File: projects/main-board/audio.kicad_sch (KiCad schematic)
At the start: 12 parts

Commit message: Updated schematics with new symbols
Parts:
- removed U10: ~, symbol symbol-library:NAU8325YG
- added U6: NAU8325YG, footprint-library:NAU8325YG, symbol symbol-library:NAU8325YG
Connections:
- net 1V8: now also U6.5 (A_VDD)
- net 3V3: now also U6.14 (SPK_VDD), U6.18 (SPK_VDD), U6.2 (SPK_VDD), U6.9 (IO_VDD)
- net GND: now also U6.13 (IO_GND), U6.16 (SPK_GND), U6.20 (SPK_GND), U6.21 (PAD), U6.3 (A_GND)
- net I2C.SCL: now also U6.11 (SCL)
- net I2C.SDA: now also U6.12 (SDA)
- net I2S.BCK: now also U6.8 (BCK)
- net I2S.DACDAT: now also U6.7 (DACDAT)
- net I2S.LRCK: now also U6.6 (LRCK)
- net I2S.MCLK: now also U6.10 (MCLK)
- net at C98.1: now also U6.4 (VREF)
- net at LS1.1: now also U6.15 (SPK_LP)
- net at LS1.2: now also U6.17 (SPK_LN)
- net at LS2.2: now also U6.1 (SPK_RP)
- net at LS2.1: now also U6.19 (SPK_RN)
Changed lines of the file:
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@@
+	)
+	(symbol
+		(lib_name "NAU8325YG_1")
+		(lib_id "symbol-library:NAU8325YG")
+		(at 152.4 63.5 0)
+		(unit 1)
+		(exclude_from_sim no)
+		(in_bom yes)
+		(on_board yes)
+		(dnp no)
+		(property "Reference" "U6"
+			(at 153.67 62.23 0)
+			(effects
+				(font
+					(size 1.27 1.27)
+				)
+			)
+		)
+		(property "Value" "NAU8325YG"
+			(at 157.48 129.54 0)
+			(effects
+				(font
+					(size 1.27 1.27)
+				)
+			)
+		)
+		(property "Footprint" "footprint-library:NAU8325YG"
+			(at 163.83 131.064 0)
+			(effects
+				(font
+					(size 1.27 1.27)
+				)
+				(hide yes)
+			)
+		)
+		(property "Datasheet" ""
+			(at 152.4 63.5 0)
+			(effects
+				(font
+					(size 1.27 1.27)
+				)
+				(hide yes)
+			)
+		)
+		(property "Description" ""
+			(at 152.4 63.5 0)
+			(effects
+				(font
+					(size 1.27 1.27)
+				)
+				(hide yes)
+			)
+		)
+		(pin "14"
+		)
+		(pin "18"
+		)
+		(pin "5"
+		)
+		(pin "9"
+		)
+		(pin "11"
+		)
+		(pin "12"
+		)
+		(pin "10"
+		)
+		(pin "6"
+		)
+		(pin "8"
+		)
+		(pin "7"
+		)
+		(pin "4"
+		)
+		(pin "15"
+		)
+		(pin "17"
+		)
+		(pin "19"
+		)
+		(pin "1"
+		)
+		(pin "3"
+		)
+		(pin "16"
+		)
+		(pin "20"
+		)
+		(pin "13"
+		)
+		(pin "21"
+		)
+		(pin "2"
+		)
+		(instances
+			(project ""
+				(path "/c621b5fd-2ef7-4a67-960d-0ffc72b1245a/8dfb54cf-5d20-4131-8758-426624cc9a00"
+					(reference "U6")
+					(unit 1)
+				)
+			)
+		)
 	)
 	(symbol
@@
 					(unit 1)
 				)
-			)
-		)
-	)
-	(symbol
-		(lib_id "symbol-library:NAU8325YG")
-		(at 152.4 63.5 0)
-		(unit 1)
-		(exclude_from_sim no)
-		(in_bom yes)
-		(on_board yes)
-		(dnp no)
-		(property "Reference" "U10"
-			(at 154.178 61.976 0)
-			(effects
-				(font
-					(size 1.27 1.27)
-				)
-			)
-		)
-		(property "Value" "~"
-			(at 159.258 61.976 0)
-			(effects
-				(font
-					(size 1.27 1.27)
-				)
-			)
-		)
-		(property "Footprint" ""
-			(at 152.4 63.5 0)
-			(effects
-				(font
-					(size 1.27 1.27)
-				)
-				(hide yes)
-			)
-		)
-		(property "Datasheet" ""
-			(at 152.4 63.5 0)
-			(effects
-				(font
-					(size 1.27 1.27)
-				)
-				(hide yes)
-			)
-		)
-		(property "Description" ""
-			(at 152.4 63.5 0)
-			(effects
-				(font
-					(size 1.27 1.27)
-				)
-				(hide yes)
-			)
-		)
-		(pin "9"
-		)
-		(pin "11"
-		)
-		(pin "12"
-		)
-		(pin "10"
-		)
-		(pin "6"
-		)
-		(pin "8"
-		)
-		(pin "7"
-		)
-		(pin "4"
-		)
-		(pin "15"
-		)
-		(pin "17"
-		)
-		(pin "19"
-		)
-		(pin "1"
-		)
-		(pin "3"
-		)
-		(pin "16"
-		)
-		(pin "20"
-		)
-		(pin "13"
-		)
-		(pin "21"
-		)
-		(pin "18"
-		)
-		(pin "5"
-		)
-		(pin "2"
-		)
-		(pin "14"
-		)
-		(instances
-			(project ""
-				(path "/c621b5fd-2ef7-4a67-960d-0ffc72b1245a/8dfb54cf-5d20-4131-8758-426624cc9a00"
-					(reference "U10")
-					(unit 1)
-				)

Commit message: Re-annotate schematics.
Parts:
- renumbered C90 to C91, C96 to C93, C93 to C94, C94 to C95, C97 to C96, C91 to C97, C95 to C98, C98 to C99, U6 to U11
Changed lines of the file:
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@@
 		(dnp no)
 		(fields_autoplaced yes)
-		(property "Reference" "#PWR0124"
+		(property "Reference" "#PWR0139"
 			(at 86.36 96.52 0)
 			(effects
@@
 			(project "main-board"
 				(path "/c621b5fd-2ef7-4a67-960d-0ffc72b1245a/8dfb54cf-5d20-4131-8758-426624cc9a00"
-					(reference "#PWR0124")
+					(reference "#PWR0139")
 					(unit 1)
 				)
@@
 		(dnp no)
 		(fields_autoplaced yes)
-		(property "Reference" "C96"
+		(property "Reference" "C93"
 			(at 88.9 85.0962 0)
 			(effects
@@
 			(project "main-board"
 				(path "/c621b5fd-2ef7-4a67-960d-0ffc72b1245a/8dfb54cf-5d20-4131-8758-426624cc9a00"
-					(reference "C96")
+					(reference "C93")
 					(unit 1)
 				)
@@
 		(dnp no)
 		(fields_autoplaced yes)
-		(property "Reference" "C98"
+		(property "Reference" "C99"
 			(at 144.78 129.5462 0)
 			(effects
@@
 			(project "main-board"
 				(path "/c621b5fd-2ef7-4a67-960d-0ffc72b1245a/8dfb54cf-5d20-4131-8758-426624cc9a00"
-					(reference "C98")
+					(reference "C99")
 					(unit 1)
 				)
@@
 		(dnp no)
 		(fields_autoplaced yes)
-		(property "Reference" "#PWR0120"
+		(property "Reference" "#PWR0136"
 			(at 67.31 68.58 0)
 			(effects
@@
 			(project ""
 				(path "/c621b5fd-2ef7-4a67-960d-0ffc72b1245a/8dfb54cf-5d20-4131-8758-426624cc9a00"
-					(reference "#PWR0120")
+					(reference "#PWR0136")
 					(unit 1)
 				)
@@
 		(dnp no)
 		(fields_autoplaced yes)
-		(property "Reference" "#PWR0121"
+		(property "Reference" "#PWR0143"
 			(at 198.12 134.62 0)
 			(effects
@@
 			(project "main-board"
 				(path "/c621b5fd-2ef7-4a67-960d-0ffc72b1245a/8dfb54cf-5d20-4131-8758-426624cc9a00"
-					(reference "#PWR0121")
+					(reference "#PWR0143")
 					(unit 1)
 				)
@@
 		(dnp no)
 		(fields_autoplaced yes)
-		(property "Reference" "C93"
+		(property "Reference" "C94"
 			(at 95.25 68.5862 0)
 			(effects
@@
 			(project "main-board"
 				(path "/c621b5fd-2ef7-4a67-960d-0ffc72b1245a/8dfb54cf-5d20-4131-8758-426624cc9a00"
-					(reference "C93")
+					(reference "C94")
 					(unit 1)
 				)
@@
 		(dnp no)
 		(fields_autoplaced yes)
-		(property "Reference" "C94"
+		(property "Reference" "C95"
 			(at 107.95 68.5862 0)
 			(effects
@@
 			(project "main-board"
 				(path "/c621b5fd-2ef7-4a67-960d-0ffc72b1245a/8dfb54cf-5d20-4131-8758-426624cc9a00"
-					(reference "C94")
+					(reference "C95")
 					(unit 1)
 				)
@@
 		(dnp no)
 		(fields_autoplaced yes)
-		(property "Reference" "C95"
+		(property "Reference" "C98"
 			(at 135.89 68.5862 0)
 			(effects
@@
 			(project "main-board"
 				(path "/c621b5fd-2ef7-4a67-960d-0ffc72b1245a/8dfb54cf-5d20-4131-8758-426624cc9a00"
-					(reference "C95")
+					(reference "C98")
 					(unit 1)
 				)
@@
 		(on_board yes)
 		(dnp no)
-		(property "Reference" "U6"
+		(property "Reference" "U11"
 			(at 153.67 62.23 0)
 			(effects
@@
 			(project ""
 				(path "/c621b5fd-2ef7-4a67-960d-0ffc72b1245a/8dfb54cf-5d20-4131-8758-426624cc9a00"
-					(reference "U6")
+					(reference "U11")
 					(unit 1)
 				)
@@
 		(dnp no)
 		(fields_autoplaced yes)
-		(property "Reference" "#PWR0127"
+		(property "Reference" "#PWR0140"
 			(at 105.41 96.52 0)
 			(effects
@@
 			(project "main-board"
 				(path "/c621b5fd-2ef7-4a67-960d-0ffc72b1245a/8dfb54cf-5d20-4131-8758-426624cc9a00"
-					(reference "#PWR0127")
+					(reference "#PWR0140")
 					(unit 1)
 				)
@@
 		(dnp no)
 		(fields_autoplaced yes)
-		(property "Reference" "#PWR0125"
+		(property "Reference" "#PWR0141"
 			(at 105.41 107.95 0)
 			(effects
@@
 			(project "main-board"
 				(path "/c621b5fd-2ef7-4a67-960d-0ffc72b1245a/8dfb54cf-5d20-4131-8758-426624cc9a00"
-					(reference "#PWR0125")
+					(reference "#PWR0141")
 					(unit 1)
 				)
@@
 		(dnp no)
 		(fields_autoplaced yes)
-		(property "Reference" "#PWR0126"
+		(property "Reference" "#PWR0142"
 			(at 142.24 140.97 0)
 			(effects
@@
 			(project "main-board"
 				(path "/c621b5fd-2ef7-4a67-960d-0ffc72b1245a/8dfb54cf-5d20-4131-8758-426624cc9a00"
-					(reference "#PWR0126")
+					(reference "#PWR0142")
 					(unit 1)
 				)
@@
 		(dnp no)
 		(fields_autoplaced yes)
-		(property "Reference" "C91"
+		(property "Reference" "C97"
 			(at 121.92 68.5862 0)
 			(effects
@@
 			(project "main-board"
 				(path "/c621b5fd-2ef7-4a67-960d-0ffc72b1245a/8dfb54cf-5d20-4131-8758-426624cc9a00"
-					(reference "C91")
+					(reference "C97")
 					(unit 1)
 				)
@@
 		(dnp no)
 		(fields_autoplaced yes)
-		(property "Reference" "#PWR0123"
+		(property "Reference" "#PWR0137"
 			(at 67.31 81.28 0)
 			(effects
@@
 			(project "main-board"
 				(path "/c621b5fd-2ef7-4a67-960d-0ffc72b1245a/8dfb54cf-5d20-4131-8758-426624cc9a00"
-					(reference "#PWR0123")
+					(reference "#PWR0137")
 					(unit 1)
 				)
@@
 		(dnp no)
 		(fields_autoplaced yes)
-		(property "Reference" "C90"
+		(property "Reference" "C91"
 			(at 69.85 68.5862 0)
 			(effects
@@
 			(project ""
 				(path "/c621b5fd-2ef7-4a67-960d-0ffc72b1245a/8dfb54cf-5d20-4131-8758-426624cc9a00"
-					(reference "C90")
+					(reference "C91")
 					(unit 1)
 				)
@@
 		(dnp no)
 		(fields_autoplaced yes)
-		(property "Reference" "#PWR0122"
+		(property "Reference" "#PWR0138"
 			(at 86.36 85.09 0)
 			(effects
@@
 			(project "main-board"
 				(path "/c621b5fd-2ef7-4a67-960d-0ffc72b1245a/8dfb54cf-5d20-4131-8758-426624cc9a00"
-					(reference "#PWR0122")
+					(reference "#PWR0138")
 					(unit 1)
 				)
@@
 		(dnp no)
 		(fields_autoplaced yes)
-		(property "Reference" "C97"
+		(property "Reference" "C96"
 			(at 107.95 96.5262 0)
 			(effects
@@
 			(project "main-board"
 				(path "/c621b5fd-2ef7-4a67-960d-0ffc72b1245a/8dfb54cf-5d20-4131-8758-426624cc9a00"
-					(reference "C97")
-					(unit 1)
-				)
+					(reference "C96")
+					(unit 1)
+				)

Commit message: Normalise capacitors
- Add capacitor parts to library.
- Replace all placeholder capacitors
  with the actual part numbers.
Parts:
- removed C91, C92, C94, C99: 4.7uF 10V, symbol Device:C_Small
- removed C93, C95, C96, C97, C98: 100nF 10V, symbol Device:C_Small
- added C91, C92, C94, C99: 4.7uF 10V, Capacitor_SMD:C_0402_1005Metric, symbol symbol-library-capacitors:CC0402MRX5R6BB475
- added C93, C95, C96, C97, C98: 100nF 10V, Capacitor_SMD:C_0402_1005Metric, symbol symbol-library-capacitors:CC0402KRX7R6BB104
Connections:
- net 1V8: now also C93.1
- net 3V3: now also C91.1, C92.1, C94.1, C95.1, C96.1, C97.1, C98.1
- net GND: now also C91.2, C92.2, C93.2, C94.2, C95.2, C96.2, C97.2, C98.2, C99.2
- net at U11.4 (VREF): now also C99.1

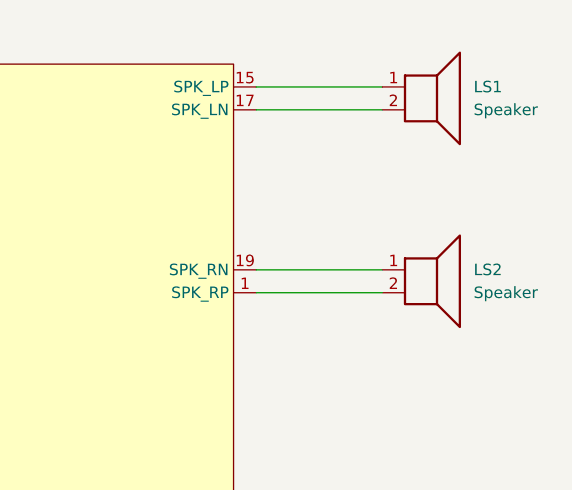
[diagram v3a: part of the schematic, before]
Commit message: Add footprints
- Inductors
- Switches
- Buttons
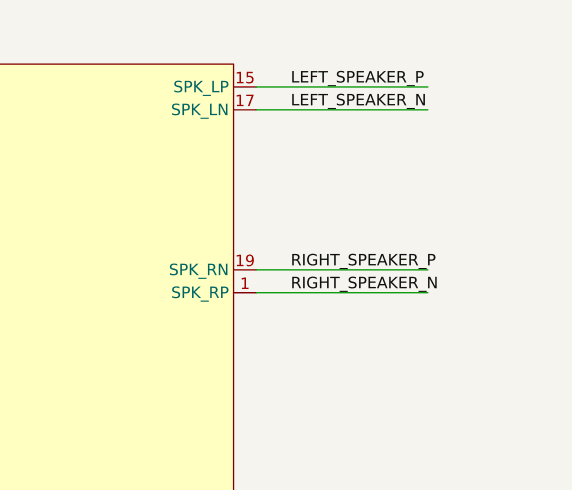
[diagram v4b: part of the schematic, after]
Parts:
- removed LS1, LS2: Speaker, symbol Device:Speaker
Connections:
- net LEFT_SPEAKER_P: now reaches U11.15 (SPK_LP)
- net LEFT_SPEAKER_N: now reaches U11.17 (SPK_LN)
- net RIGHT_SPEAKER_N: now reaches U11.1 (SPK_RP)
- net RIGHT_SPEAKER_P: now reaches U11.19 (SPK_RN)
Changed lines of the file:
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@@
+	(wire
+		(pts
+			(xy 196.85 88.9) (xy 215.9 88.9)
+		)
+		(stroke
+			(width 0)
+			(type default)
+		)
+	)
 	(wire
 		(pts
@@
 	(wire
 		(pts
+			(xy 196.85 86.36) (xy 215.9 86.36)
+		)
+		(stroke
+			(width 0)
+			(type default)
+		)
+	)
+	(wire
+		(pts
 			(xy 92.71 66.04) (xy 92.71 67.31)
 		)
@@
 	(wire
 		(pts
+			(xy 196.85 68.58) (xy 215.9 68.58)
+		)
+		(stroke
+			(width 0)
+			(type default)
+		)
+	)
+	(wire
+		(pts
 			(xy 105.41 66.04) (xy 105.41 67.31)
 		)
@@
 	(wire
 		(pts
-			(xy 210.82 88.9) (xy 196.85 88.9)
-		)
-		(stroke
-			(width 0)
-			(type default)
-		)
-	)
-	(wire
-		(pts
 			(xy 142.24 127) (xy 142.24 128.27)
 		)
@@
 	(wire
 		(pts
-			(xy 210.82 86.36) (xy 196.85 86.36)
-		)
-		(stroke
-			(width 0)
-			(type default)
-		)
-	)
-	(wire
-		(pts
-			(xy 210.82 68.58) (xy 196.85 68.58)
-		)
-		(stroke
-			(width 0)
-			(type default)
-		)
-	)
-	(wire
-		(pts
 			(xy 119.38 66.04) (xy 133.35 66.04)
 		)
@@
 	(wire
 		(pts
-			(xy 210.82 66.04) (xy 196.85 66.04)
+			(xy 196.85 66.04) (xy 215.9 66.04)
 		)
 		(stroke
@@
 		)
 	)
+	(label "LEFT_SPEAKER_N"
+		(at 200.66 68.58 0)
+		(effects
+			(font
+				(size 1.27 1.27)
+			)
+			(justify left bottom)
+		)
+	)
 	(label "I2C{SCL SDA}"
 		(at 105.41 111.76 0)
@@
 		)
 	)
+	(label "RIGHT_SPEAKER_P"
+		(at 200.66 86.36 0)
+		(effects
+			(font
+				(size 1.27 1.27)
+			)
+			(justify left bottom)
+		)
+	)
 	(label "I2S.BCK"
 		(at 135.89 119.38 0)
@@
 		)
 	)
+	(label "LEFT_SPEAKER_P"
+		(at 200.66 66.04 0)
+		(effects
+			(font
+				(size 1.27 1.27)
+			)
+			(justify left bottom)
+		)
+	)
 	(label "I2C.SDA"
 		(at 135.89 109.22 0)
@@
 	(label "I2C.SCL"
 		(at 135.89 106.68 0)
+		(effects
+			(font
+				(size 1.27 1.27)
+			)
+			(justify left bottom)
+		)
+	)
+	(label "RIGHT_SPEAKER_N"
+		(at 200.66 88.9 0)
 		(effects
 			(font
@@
 		(dnp no)
 		(fields_autoplaced yes)
-		(property "Reference" "#PWR0137"
+		(property "Reference" "#PWR0138"
 			(at 86.36 96.52 0)
 			(effects
@@
 			(project "main-board"
 				(path "/c621b5fd-2ef7-4a67-960d-0ffc72b1245a/8dfb54cf-5d20-4131-8758-426624cc9a00"
-					(reference "#PWR0137")
+					(reference "#PWR0138")
 					(unit 1)
 				)
@@
 		(dnp no)
 		(fields_autoplaced yes)
-		(property "Reference" "#PWR0134"
+		(property "Reference" "#PWR0135"
 			(at 67.31 68.58 0)
 			(effects
@@
 			(project ""
 				(path "/c621b5fd-2ef7-4a67-960d-0ffc72b1245a/8dfb54cf-5d20-4131-8758-426624cc9a00"
-					(reference "#PWR0134")
+					(reference "#PWR0135")
 					(unit 1)
 				)
@@
 		(dnp no)
 		(fields_autoplaced yes)
-		(property "Reference" "#PWR0141"
+		(property "Reference" "#PWR0142"
 			(at 198.12 134.62 0)
 			(effects
@@
 			(project "main-board"
 				(path "/c621b5fd-2ef7-4a67-960d-0ffc72b1245a/8dfb54cf-5d20-4131-8758-426624cc9a00"
-					(reference "#PWR0141")
+					(reference "#PWR0142")
 					(unit 1)
 				)
@@
 	)
 	(symbol
-		(lib_id "Device:Speaker")
-		(at 215.9 66.04 0)
-		(unit 1)
-		(exclude_from_sim no)
-		(in_bom yes)
-		(on_board yes)
-		(dnp no)
-		(fields_autoplaced yes)
-		(property "Reference" "LS1"
-			(at 220.98 66.0399 0)
-			(effects
-				(font
-					(size 1.27 1.27)
-				)
-				(justify left)
-			)
-		)
-		(property "Value" "Speaker"
-			(at 220.98 68.5799 0)
-			(effects
-				(font
-					(size 1.27 1.27)
-				)
-				(justify left)
-			)
-		)
-		(property "Footprint" ""
-			(at 215.9 71.12 0)
-			(effects
-				(font
-					(size 1.27 1.27)
-				)
-				(hide yes)
-			)
-		)
-		(property "Datasheet" "~"
-			(at 215.646 67.31 0)
-			(effects
-				(font
-					(size 1.27 1.27)
-				)
-				(hide yes)
-			)
-		)
-		(property "Description" "Speaker"
-			(at 215.9 66.04 0)
-			(effects
-				(font
-					(size 1.27 1.27)
-				)
-				(hide yes)
-			)
-		)
-		(pin "1"
-		)
-		(pin "2"
-		)
-		(instances
-			(project ""
-				(path "/c621b5fd-2ef7-4a67-960d-0ffc72b1245a/8dfb54cf-5d20-4131-8758-426624cc9a00"
-					(reference "LS1")
-					(unit 1)
-				)
-			)
-		)
-	)
-	(symbol
 		(lib_name "NAU8325YG_1")
 		(lib_id "symbol-library:NAU8325YG")
@@
 		(dnp no)
 		(fields_autoplaced yes)
-		(property "Reference" "#PWR0138"
+		(property "Reference" "#PWR0139"
 			(at 105.41 96.52 0)
 			(effects
@@
 			(project "main-board"
 				(path "/c621b5fd-2ef7-4a67-960d-0ffc72b1245a/8dfb54cf-5d20-4131-8758-426624cc9a00"
-					(reference "#PWR0138")
+					(reference "#PWR0139")
 					(unit 1)
 				)
@@
 		(dnp no)
 		(fields_autoplaced yes)
-		(property "Reference" "#PWR0139"
+		(property "Reference" "#PWR0140"
 			(at 105.41 107.95 0)
 			(effects
@@
 			(project "main-board"
 				(path "/c621b5fd-2ef7-4a67-960d-0ffc72b1245a/8dfb54cf-5d20-4131-8758-426624cc9a00"
-					(reference "#PWR0139")
+					(reference "#PWR0140")
 					(unit 1)
 				)
@@
 		(dnp no)
 		(fields_autoplaced yes)
-		(property "Reference" "#PWR0140"
+		(property "Reference" "#PWR0141"
 			(at 142.24 140.97 0)
 			(effects
@@
 			(project "main-board"
 				(path "/c621b5fd-2ef7-4a67-960d-0ffc72b1245a/8dfb54cf-5d20-4131-8758-426624cc9a00"
-					(reference "#PWR0140")
+					(reference "#PWR0141")
 					(unit 1)
 				)
@@
 		(dnp no)
 		(fields_autoplaced yes)
-		(property "Reference" "#PWR0135"
+		(property "Reference" "#PWR0136"
 			(at 67.31 81.28 0)
 			(effects
@@
 			(project "main-board"
 				(path "/c621b5fd-2ef7-4a67-960d-0ffc72b1245a/8dfb54cf-5d20-4131-8758-426624cc9a00"
-					(reference "#PWR0135")
+					(reference "#PWR0136")
 					(unit 1)
 				)
@@
 		(dnp no)
 		(fields_autoplaced yes)
-		(property "Reference" "#PWR0136"
+		(property "Reference" "#PWR0137"
 			(at 86.36 85.09 0)
 			(effects
@@
 			(project "main-board"
 				(path "/c621b5fd-2ef7-4a67-960d-0ffc72b1245a/8dfb54cf-5d20-4131-8758-426624cc9a00"
-					(reference "#PWR0136")
+					(reference "#PWR0137")
 					(unit 1)
 				)
-			)
-		)
-	)
-	(symbol
-		(lib_id "Device:Speaker")
-		(at 215.9 86.36 0)
-		(unit 1)
-		(exclude_from_sim no)
-		(in_bom yes)
-		(on_board yes)
-		(dnp no)
-		(fields_autoplaced yes)
-		(property "Reference" "LS2"
-			(at 220.98 86.3599 0)
-			(effects
-				(font
-					(size 1.27 1.27)
-				)
-				(justify left)
-			)
-		)
-		(property "Value" "Speaker"
-			(at 220.98 88.8999 0)
-			(effects
-				(font
-					(size 1.27 1.27)
-				)
-				(justify left)
-			)
-		)
-		(property "Footprint" ""
-			(at 215.9 91.44 0)
-			(effects
-				(font
-					(size 1.27 1.27)
-				)
-				(hide yes)
-			)
-		)
-		(property "Datasheet" "~"
-			(at 215.646 87.63 0)
-			(effects
-				(font
-					(size 1.27 1.27)
-				)
-				(hide yes)
-			)
-		)
-		(property "Description" "Speaker"
-			(at 215.9 86.36 0)
-			(effects
-				(font
-					(size 1.27 1.27)
-				)
-				(hide yes)
-			)
-		)
-		(pin "1"
-		)
-		(pin "2"
-		)
-		(instances
-			(project "main-board"
-				(path "/c621b5fd-2ef7-4a67-960d-0ffc72b1245a/8dfb54cf-5d20-4131-8758-426624cc9a00"
-					(reference "LS2")
-					(unit 1)
-				)

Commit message: WIP splitting main board into 3
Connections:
- net LEFT_SPEAKER_N renamed LEFT_SPEAKER.N
- net LEFT_SPEAKER_P renamed LEFT_SPEAKER.P
- net RIGHT_SPEAKER_N renamed RIGHT_SPEAKER.N
- net RIGHT_SPEAKER_P renamed RIGHT_SPEAKER.P
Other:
- moved on the sheet: C91, C92, C93, C94, C95, C96, C97, C98, C99, U11
